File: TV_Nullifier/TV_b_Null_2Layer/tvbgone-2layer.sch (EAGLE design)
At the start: 18 parts, among them IC1 ATTINY85V-10S, Q1 BC857AT115, Q2 PMBT3904VS_DUAL_NPN, Y1_8MHZ RESONATOR

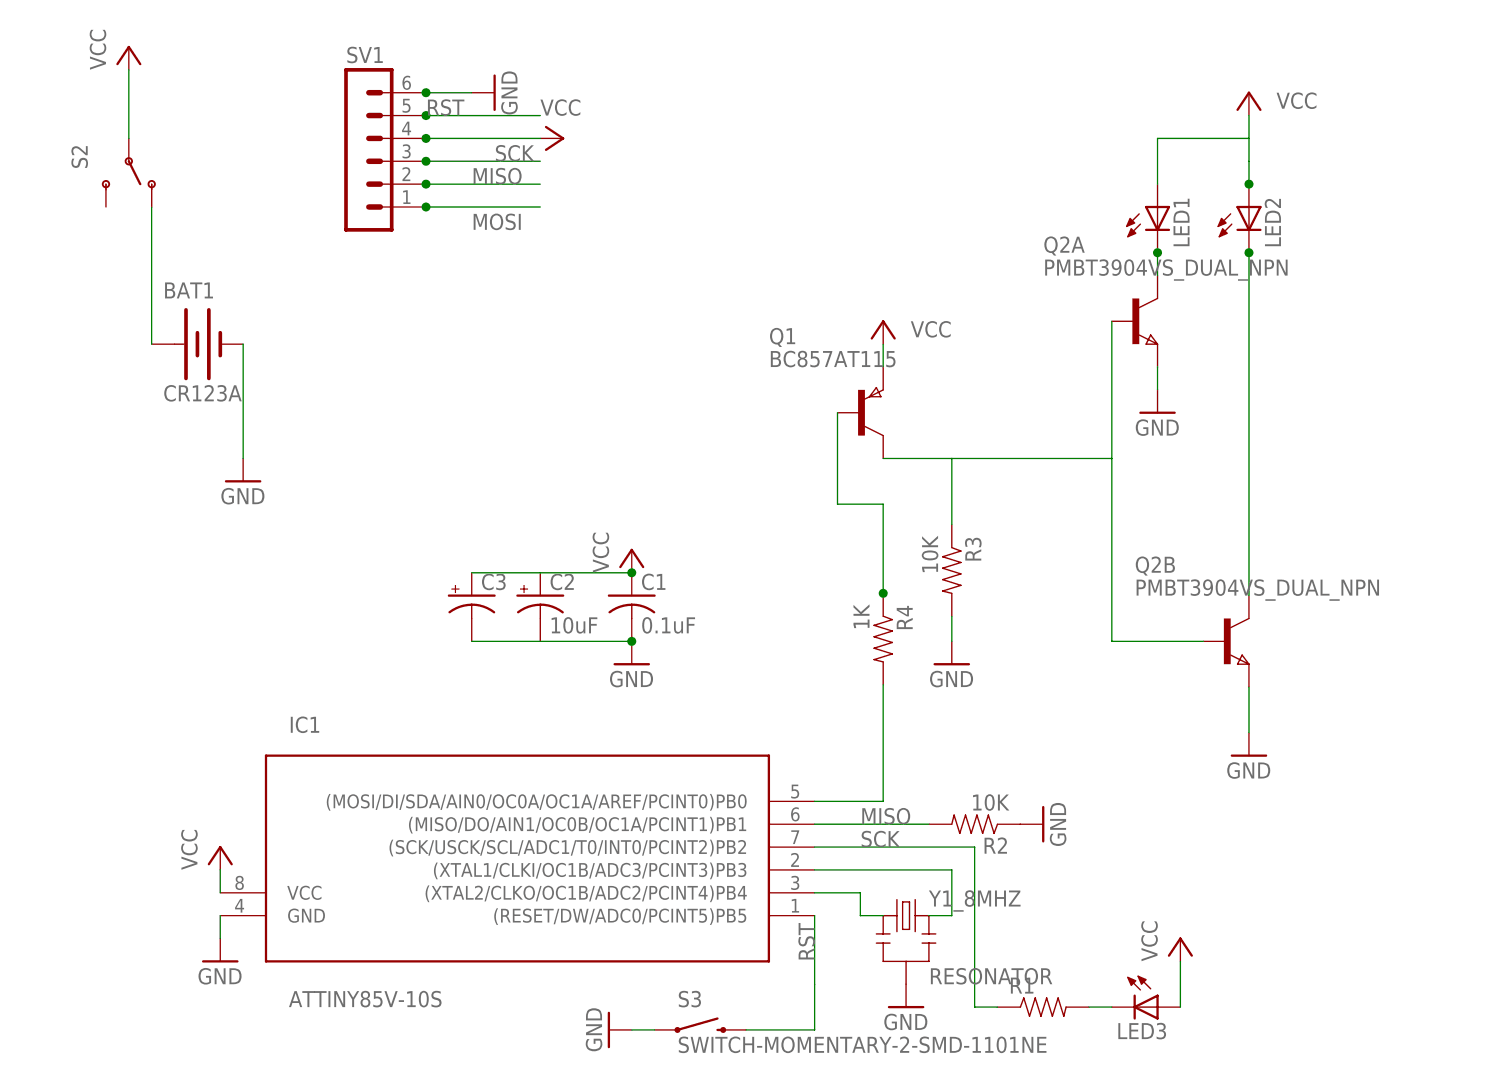
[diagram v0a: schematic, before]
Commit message: 
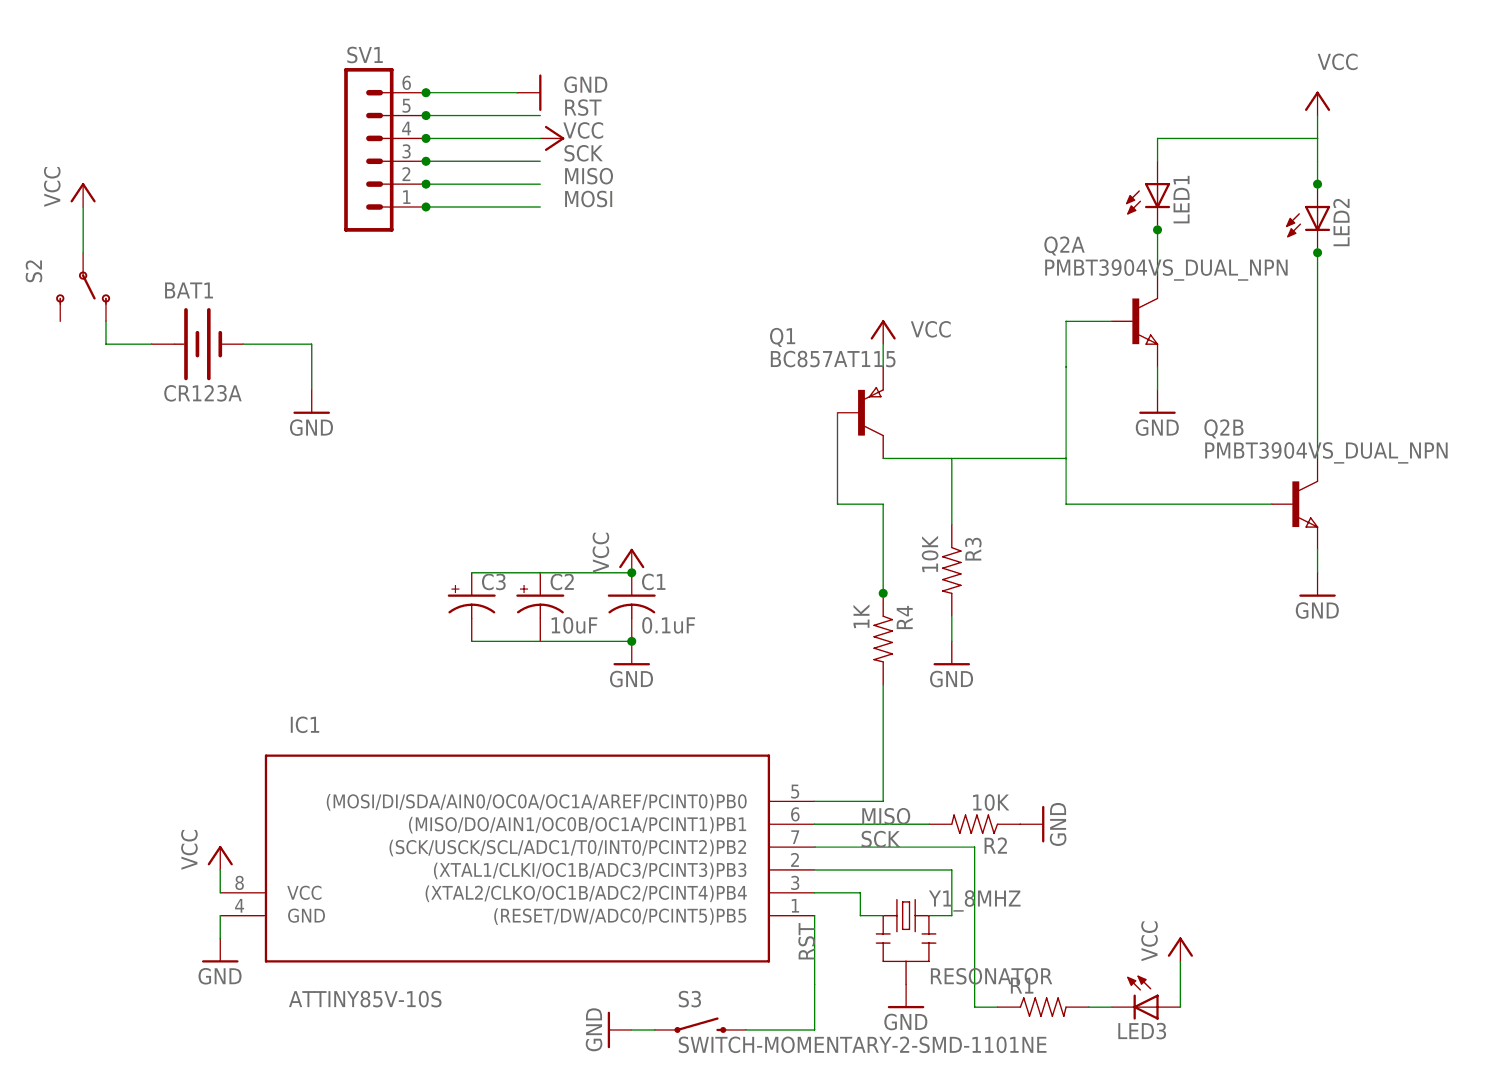
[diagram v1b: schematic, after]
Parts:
- BAT1: device tvbgone-adj:BATTERYCR123A -> tvbgone-2layer:TVBGONE-ADJ_BATTERYCR123A
- Y1_8MHZ: device SparkFun:RESONATORSMD -> tvbgone-2layer:SPARKFUN_RESONATORSMD
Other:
- moved on the sheet: LED1, LED2, Q2B, S2

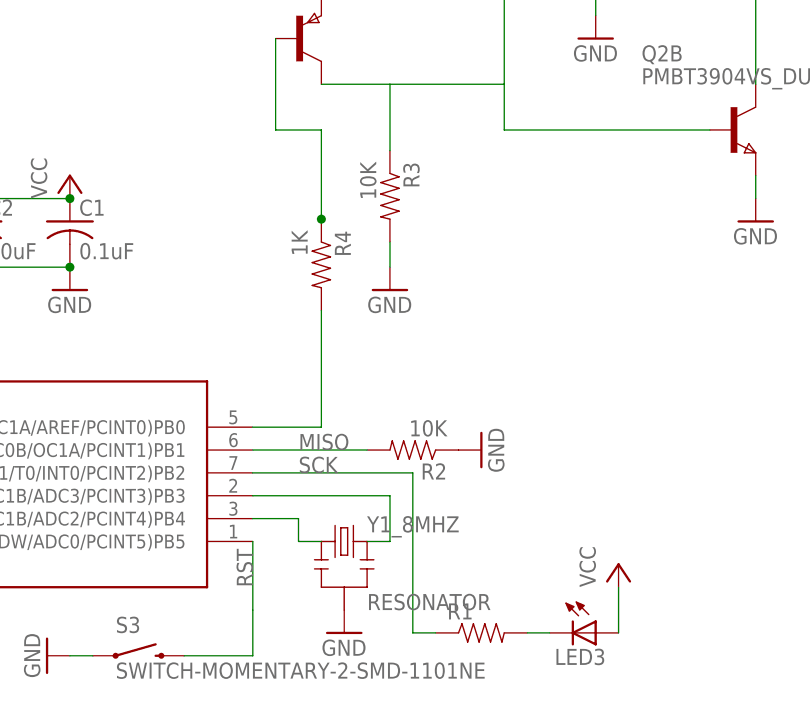
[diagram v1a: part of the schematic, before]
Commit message: 
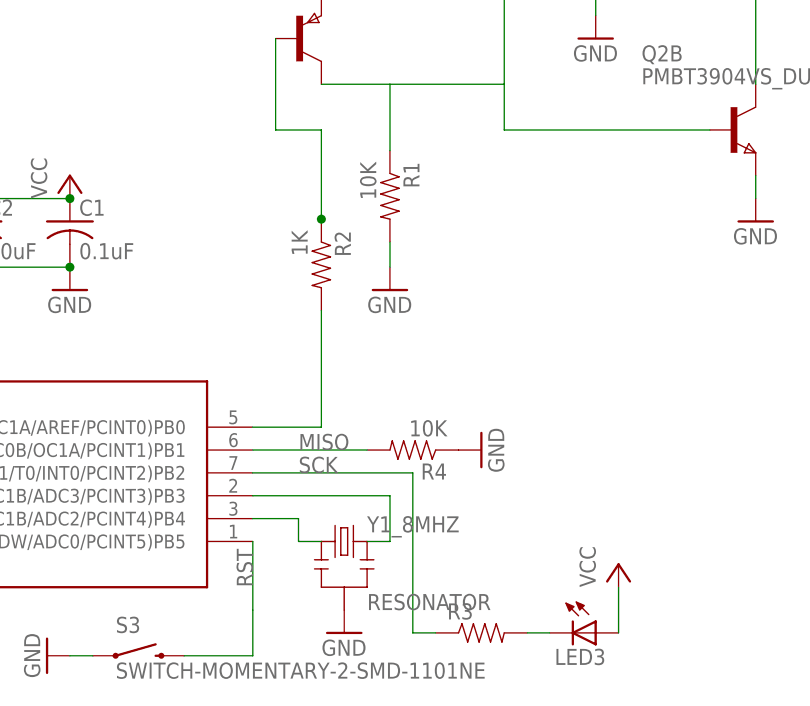
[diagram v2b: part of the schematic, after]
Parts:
- R1: value 1.5K -> 10K
- R2: value 10K -> 1K
- R3: value 10K -> 1.5K
- R4: value 1K -> 10K
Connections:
- net GND: now also R1.2, R4.1; no longer R2.1, R3.2
- net MISO: now also R4.2; no longer R2.2
- net MOSI: now also R2.2; no longer R4.2
- net N$3: now also R3.2; no longer R1.2
- net N$6: now also R2.1; no longer R4.1
- net N$9: now also R1.1; no longer R3.1
- net SCK: now also R3.1; no longer R1.1
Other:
- moved on the sheet: R1, R2, R3, R4
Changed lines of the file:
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@@
 <part name="LED3" library="minimidi" deviceset="LED" device="CHIPLED_0603"/>
 <part name="P+6" library="supply1" deviceset="VCC" device=""/>
-<part name="R1" library="SparkFun" deviceset="RESISTOR" device="" value="1.5K"/>
+<part name="R3" library="SparkFun" deviceset="RESISTOR" device="" value="1.5K"/>
 <part name="GND9" library="supply1" deviceset="GND" device=""/>
 <part name="GND10" library="supply1" deviceset="GND" device=""/>
-<part name="R3" library="SparkFun" deviceset="RESISTOR" device="" value="10K"/>
-<part name="R2" library="SparkFun" deviceset="RESISTOR" device="" value="10K"/>
+<part name="R1" library="SparkFun" deviceset="RESISTOR" device="" value="10K"/>
+<part name="R4" library="SparkFun" deviceset="RESISTOR" device="" value="10K"/>
 <part name="GND11" library="supply1" deviceset="GND" device=""/>
 <part name="SV1" library="NSL" deviceset="CON-LSTB_MA06-1" device=""/>
@@
 <part name="LED1" library="tvbgone3" deviceset="LED" device="SIDEIR"/>
 <part name="LED2" library="tvbgone3" deviceset="LED" device="SIDEIR"/>
-<part name="R4" library="SparkFun" deviceset="RESISTOR" device="" value="1K"/>
+<part name="R2" library="SparkFun" deviceset="RESISTOR" device="" value="1K"/>
 <part name="S2" library="SparkFun-Electromechanical" deviceset="SWITCH-SPDT" device="-SMD-A"/>
 <part name="S3" library="SparkFun-Electromechanical" deviceset="SWITCH-MOMENTARY-2" device="-SMD-1101NE"/>
@@
 <attribute name="VALUE" x="142.24" y="55.88" size="1.778" layer="96" rot="R90"/>
 </instance>
-<instance part="R1" gate="G$1" x="129.54" y="50.8" smashed="yes">
+<instance part="R3" gate="G$1" x="129.54" y="50.8" smashed="yes">
 <attribute name="NAME" x="125.73" y="52.2986" size="1.778" layer="95"/>
 </instance>
@@
 <attribute name="VALUE" x="76.2" y="152.4" size="1.778" layer="96"/>
 </instance>
-<instance part="R3" gate="G$1" x="119.38" y="99.314" smashed="yes" rot="R270">
+<instance part="R1" gate="G$1" x="119.38" y="99.314" smashed="yes" rot="R270">
 <attribute name="NAME" x="120.8786" y="103.124" size="1.778" layer="95" rot="R270"/>
 <attribute name="VALUE" x="116.078" y="103.124" size="1.778" layer="96" rot="R270"/>
 </instance>
-<instance part="R2" gate="G$1" x="121.92" y="71.12" smashed="yes" rot="R180">
+<instance part="R4" gate="G$1" x="121.92" y="71.12" smashed="yes" rot="R180">
 <attribute name="NAME" x="125.73" y="69.6214" size="1.778" layer="95" rot="R180"/>
 <attribute name="VALUE" x="125.73" y="74.422" size="1.778" layer="96" rot="R180"/>
@@
 <attribute name="VALUE" x="165.735" y="135.128" size="1.778" layer="96" rot="R90"/>
 </instance>
-<instance part="R4" gate="G$1" x="111.76" y="91.694" smashed="yes" rot="R270">
+<instance part="R2" gate="G$1" x="111.76" y="91.694" smashed="yes" rot="R270">
 <attribute name="NAME" x="113.2586" y="95.504" size="1.778" layer="95" rot="R270"/>
 <attribute name="VALUE" x="108.458" y="95.504" size="1.778" layer="96" rot="R270"/>
@@
 </segment>
 <segment>
-<pinref part="R2" gate="G$1" pin="1"/>
+<pinref part="R4" gate="G$1" pin="1"/>
 <pinref part="GND11" gate="1" pin="GND"/>
 </segment>
@@
 <segment>
 <wire x1="119.38" y1="94.234" x2="119.38" y2="91.44" width="0.1524" layer="91"/>
-<pinref part="R3" gate="G$1" pin="2"/>
+<pinref part="R1" gate="G$1" pin="2"/>
 <pinref part="GND7" gate="1" pin="GND"/>
 </segment>
@@
 <wire x1="134.62" y1="50.8" x2="137.16" y2="50.8" width="0.1524" layer="91"/>
 <pinref part="LED3" gate="G$1" pin="C"/>
-<pinref part="R1" gate="G$1" pin="2"/>
+<pinref part="R3" gate="G$1" pin="2"/>
 </segment>
 </net>
@@
 <wire x1="111.76" y1="86.614" x2="111.76" y2="73.66" width="0.1524" layer="91"/>
 <pinref part="IC1" gate="G$1" pin="(MOSI/DI/SDA/AIN0/OC0A/OC1A/AREF/PCINT0)PB0"/>
-<pinref part="R4" gate="G$1" pin="2"/>
+<pinref part="R2" gate="G$1" pin="2"/>
 </segment>
 </net>
@@
 <label x="109.22" y="71.12" size="1.778" layer="95"/>
 <pinref part="IC1" gate="G$1" pin="(MISO/DO/AIN1/OC0B/OC1A/PCINT1)PB1"/>
-<pinref part="R2" gate="G$1" pin="2"/>
+<pinref part="R4" gate="G$1" pin="2"/>
 </segment>
 </net>
@@
 <label x="109.22" y="68.58" size="1.778" layer="95"/>
 <pinref part="IC1" gate="G$1" pin="(SCK/USCK/SCL/ADC1/T0/INT0/PCINT2)PB2"/>
-<pinref part="R1" gate="G$1" pin="1"/>
+<pinref part="R3" gate="G$1" pin="1"/>
 </segment>
 </net>
@@
 <junction x="111.76" y="96.774"/>
 <pinref part="Q1" gate="A" pin="B"/>
-<pinref part="R4" gate="G$1" pin="1"/>
+<pinref part="R2" gate="G$1" pin="1"/>
 </segment>
 </net>
@@
 <wire x1="119.38" y1="111.76" x2="132.08" y2="111.76" width="0.1524" layer="91"/>
 <wire x1="119.38" y1="104.394" x2="119.38" y2="111.76" width="0.1524" layer="91"/>
-<pinref part="R3" gate="G$1" pin="1"/>
+<pinref part="R1" gate="G$1" pin="1"/>
 <pinref part="Q2" gate="A" pin="B"/>
 <wire x1="137.16" y1="127" x2="132.08" y2="127" width="0.1524" layer="91"/>
